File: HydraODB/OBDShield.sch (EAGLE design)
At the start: 10 parts, among them J1 HYDRABUS_SHIELD_CON_HEADER_2X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, J2 HYDRABUS_SHIELD_CON_HEADER_2X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, J3 HYDRABUS_SHIELD_CON_HEADER_2X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, U1 SN65HVD233DG4, U2 SN65HVD233DG4

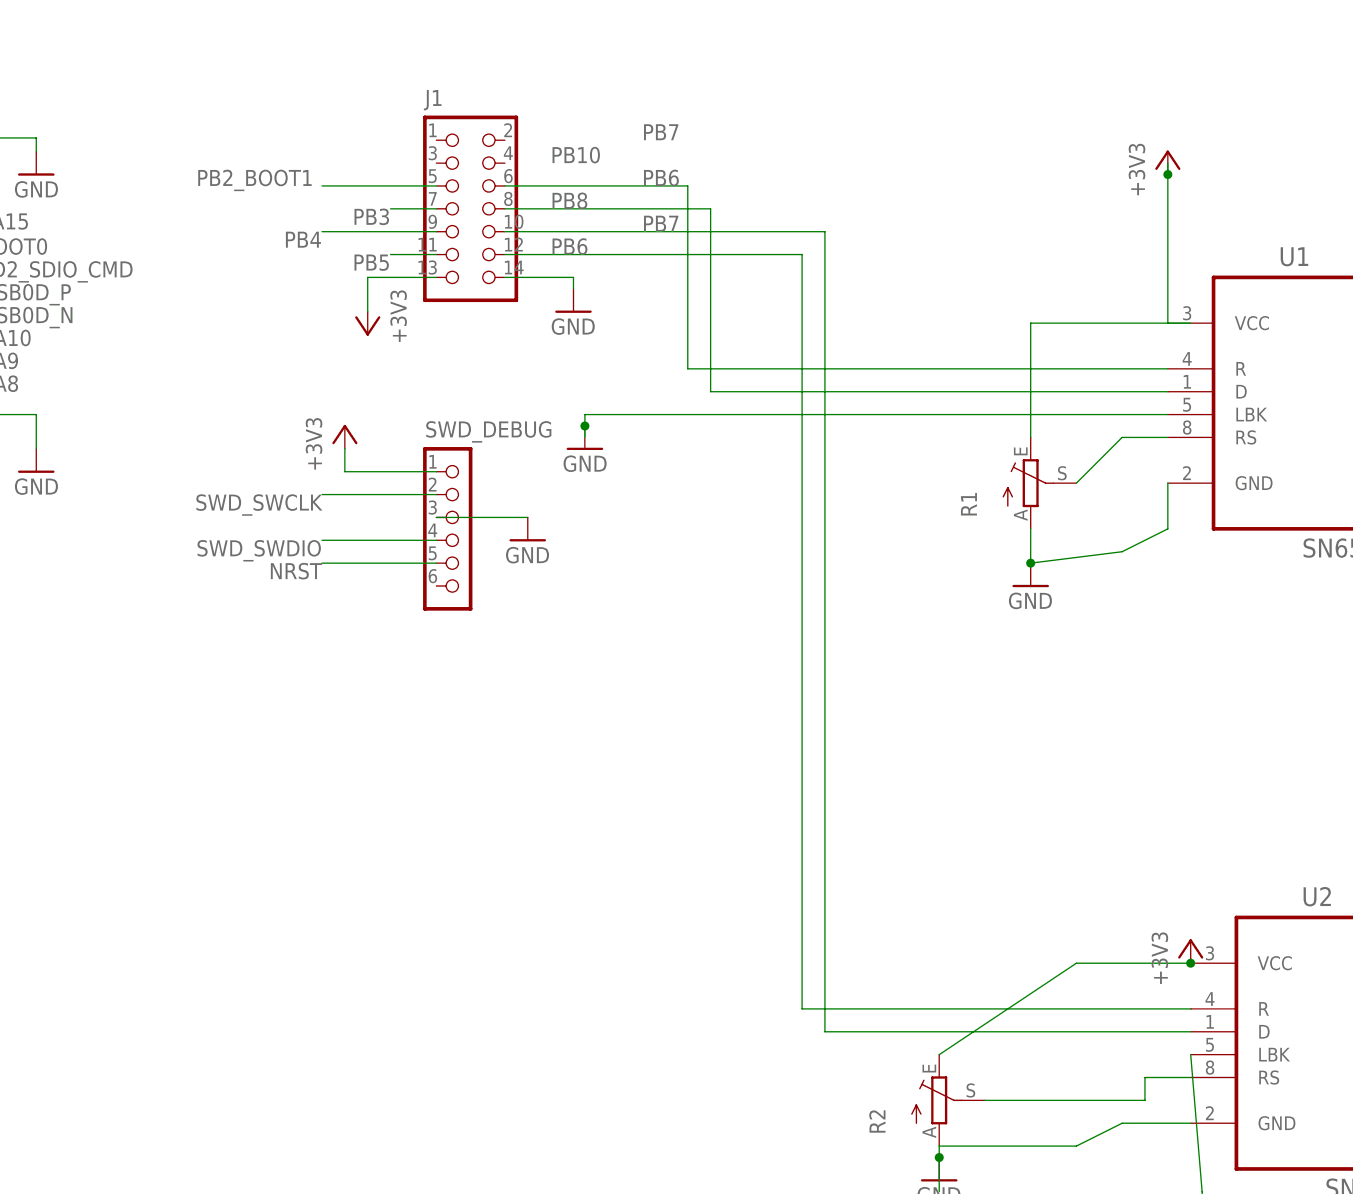
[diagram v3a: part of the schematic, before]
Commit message: Schema correction
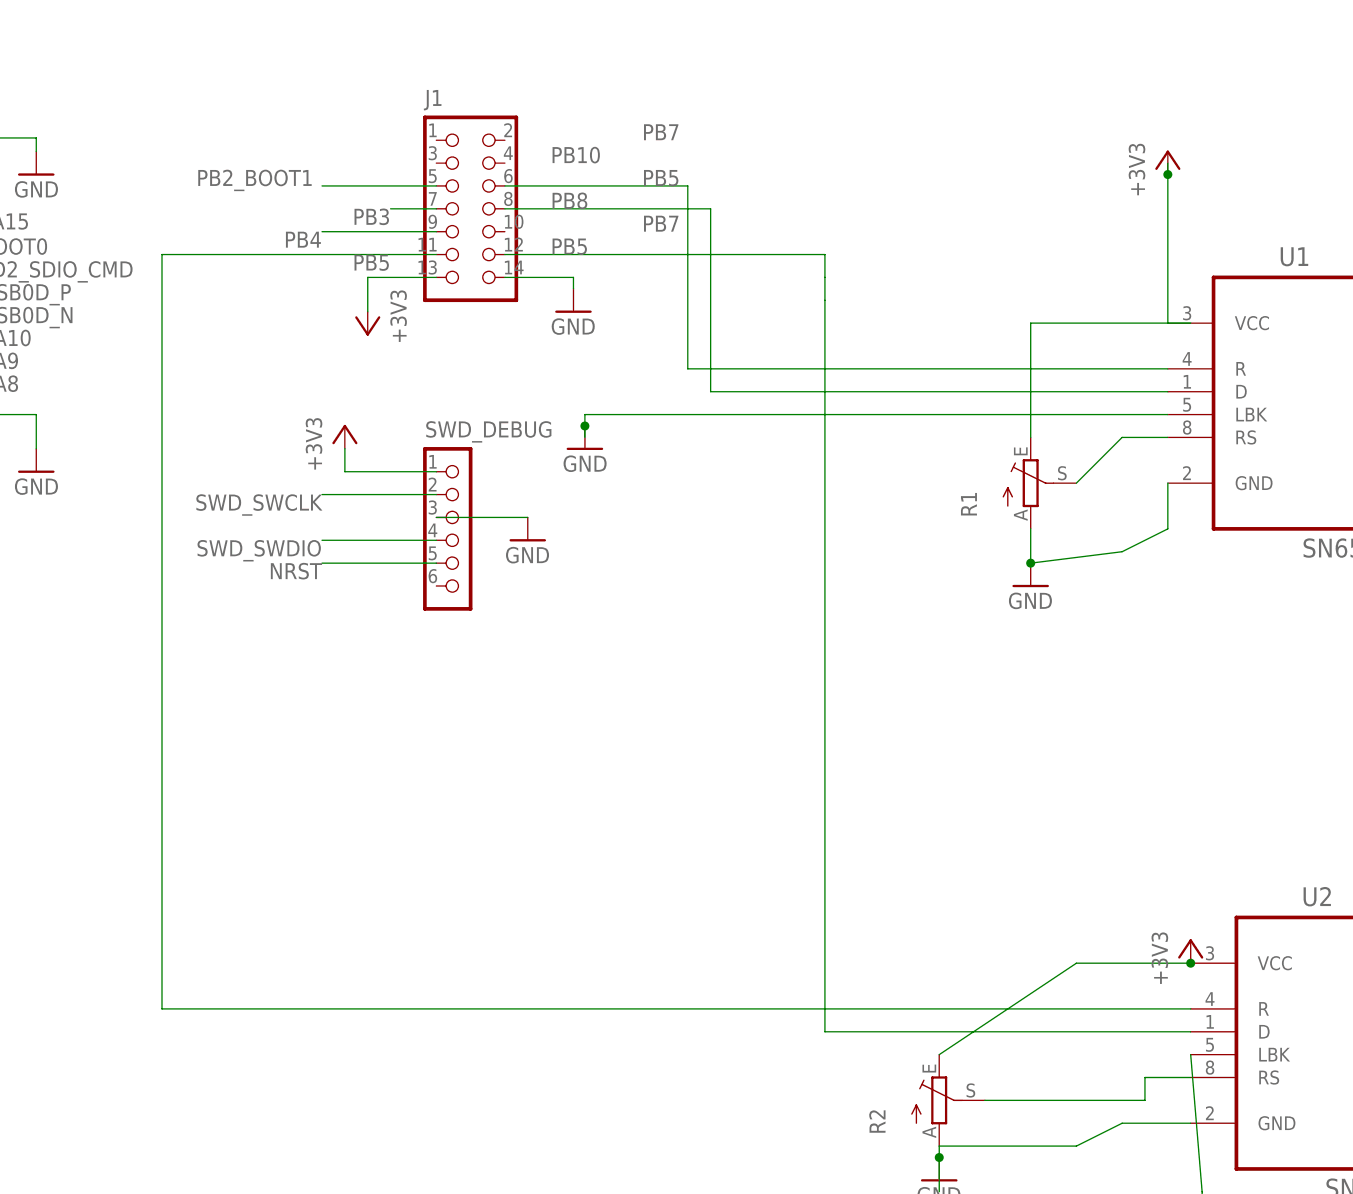
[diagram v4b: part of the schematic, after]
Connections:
- removed net PB6: J1.12, U2.R
- net PB5: now also U2.R
- net PB7: now also J1.12; no longer J1.10
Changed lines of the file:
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@@
-</segment>
-</net>
-<net name="PB5" class="0">
-<segment>
-<wire x1="76.2" y1="121.92" x2="71.12" y2="121.92" width="0.1524" layer="91"/>
-<label x="71.12" y="121.92" size="1.778" layer="95" rot="R180"/>
-<pinref part="J1" gate="J" pin="11"/>
 </segment>
 </net>
@@
 </segment>
 </net>
-<net name="PB6" class="0">
-<segment>
-<label x="99.06" y="129.54" size="1.778" layer="95"/>
-<pinref part="U2" gate="A" pin="R"/>
-<wire x1="160.02" y1="38.1" x2="116.84" y2="38.1" width="0.1524" layer="91"/>
-<wire x1="116.84" y1="38.1" x2="116.84" y2="121.92" width="0.1524" layer="91"/>
-<label x="88.9" y="121.92" size="1.778" layer="95"/>
-<pinref part="J1" gate="J" pin="12"/>
-<wire x1="116.84" y1="121.92" x2="83.82" y2="121.92" width="0.1524" layer="91"/>
-</segment>
-</net>
 <net name="PB7" class="0">
 <segment>
@@
 <pinref part="U2" gate="A" pin="D"/>
 <wire x1="160.02" y1="35.56" x2="119.38" y2="35.56" width="0.1524" layer="91"/>
-<wire x1="119.38" y1="35.56" x2="119.38" y2="124.46" width="0.1524" layer="91"/>
+<wire x1="119.38" y1="35.56" x2="119.38" y2="116.84" width="0.1524" layer="91"/>
 <label x="99.06" y="124.46" size="1.778" layer="95"/>
-<pinref part="J1" gate="J" pin="10"/>
-<wire x1="119.38" y1="124.46" x2="83.82" y2="124.46" width="0.1524" layer="91"/>
+<pinref part="J1" gate="J" pin="12"/>
+<wire x1="119.38" y1="116.84" x2="119.38" y2="119.38" width="0.1524" layer="91"/>
+<wire x1="83.82" y1="121.92" x2="119.38" y2="121.92" width="0.1524" layer="91"/>
+<wire x1="119.38" y1="121.92" x2="119.38" y2="119.38" width="0.1524" layer="91"/>
 </segment>
 </net>
+<net name="PB5" class="0">
+<segment>
+<label x="99.06" y="129.54" size="1.778" layer="95"/>
+<pinref part="U2" gate="A" pin="R"/>
+<wire x1="160.02" y1="38.1" x2="45.72" y2="38.1" width="0.1524" layer="91"/>
+<label x="88.9" y="121.92" size="1.778" layer="95"/>
+<wire x1="45.72" y1="38.1" x2="45.72" y2="121.92" width="0.1524" layer="91"/>
+<label x="71.12" y="121.92" size="1.778" layer="95" rot="R180"/>
+<pinref part="J1" gate="J" pin="11"/>
+<wire x1="45.72" y1="121.92" x2="76.2" y2="121.92" width="0.1524" layer="91"/>
+</segment>
+</net>

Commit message: Mistake :-D
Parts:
- added JP1, JP2: (no value), jumper:JP1E
- added LPWR, LRXCAN1, LRXCAN2, LTXCAN1, LTXCAN2: (no value), led:LEDCHIPLED_0603
- added R3, R4, R5, R6, R7, R8, R9: (no value), resistor:R-EU_R0603
- IC1: value (none) -> LM317MABDT; device v-reg:78XXS -> v-reg:LM317MABDT
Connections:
- new net N$13: LTXCAN1.A, R5.2
- new net N$14: LPWR.A, R3.1
- new net N$15: R3.2
- new net N$16: JP2.1, R9.2
- new net N$19: JP1.1, R8.2
- new net N$7: LRXCAN1.A, R4.2
- new net PB11: J1.4, R9.1, U2.D
- new net PB6: J1.12
- new net PB9: J1.2, JP2.2, U2.R
- net +12V: now also SV1.7, SV1.8
- net GND: now also IC1.ADJ, LPWR.C, LTXCAN1.C; no longer IC1.GND
- net PB10: now also J1.6, JP1.2, R5.1; no longer J1.8
- net PB5: no longer U2.R
- net PB7: now also J1.10; no longer J1.12, U2.D
- net PB8: now also J1.8, R4.1, R8.1; no longer J1.6
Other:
- moved on the sheet: R2, SV1

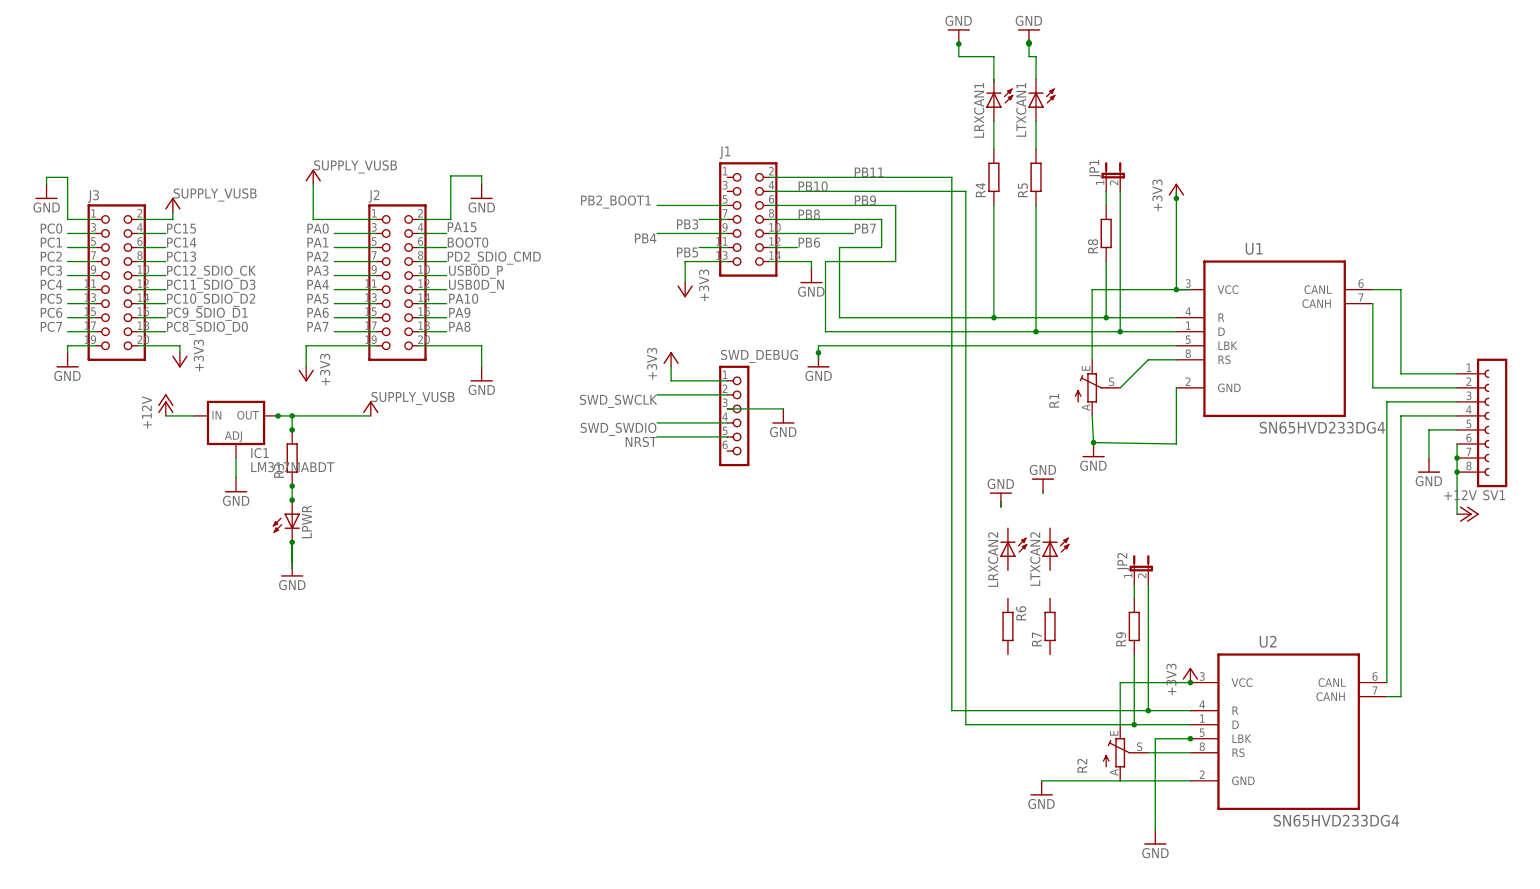
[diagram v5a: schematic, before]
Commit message: Decoupling caps, user button and different mistakes
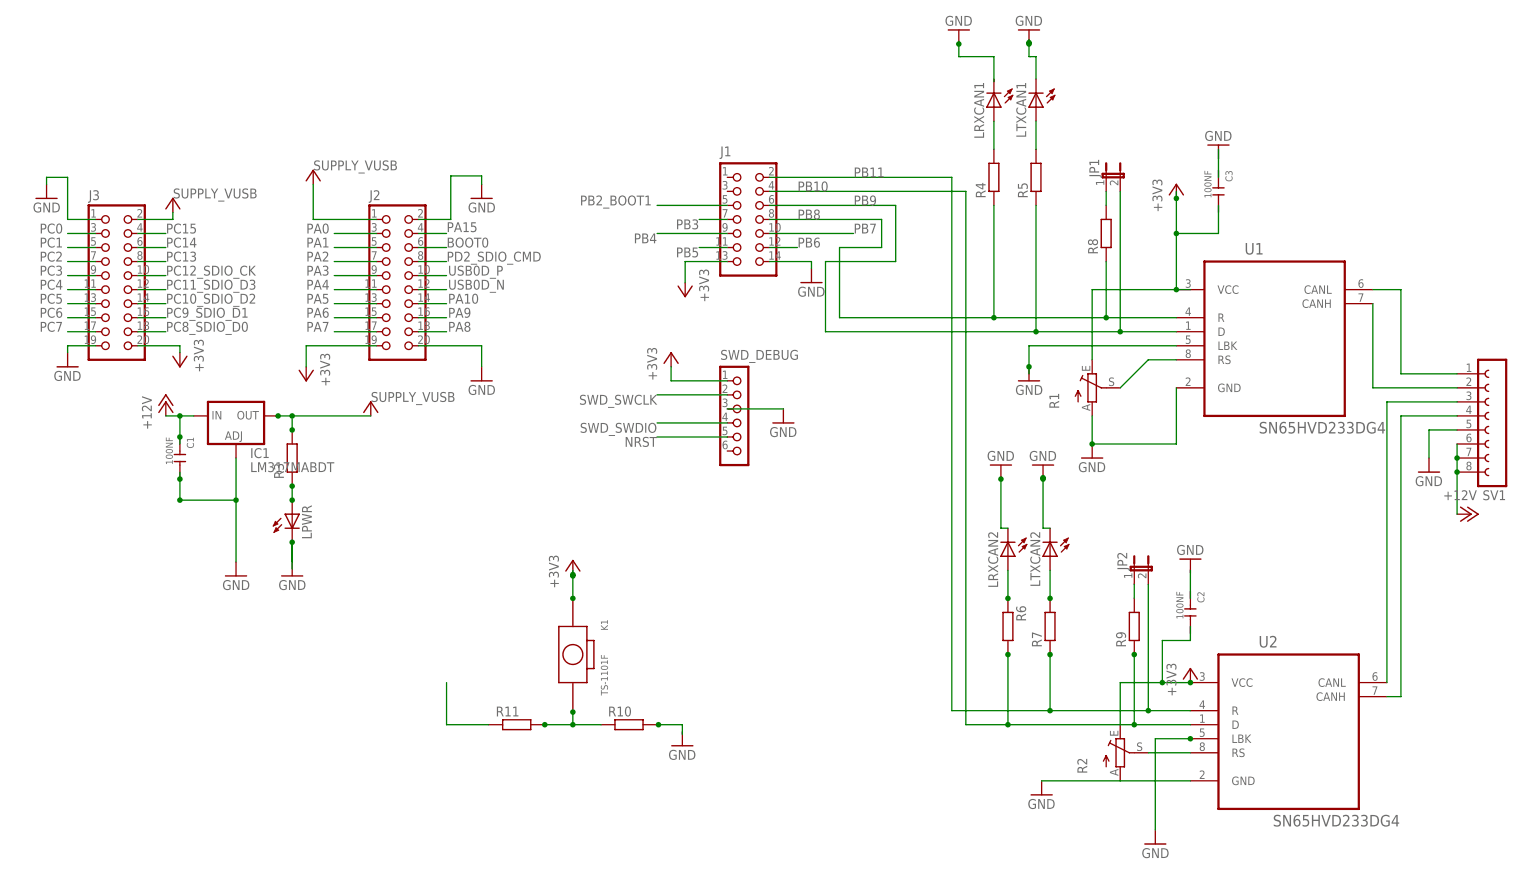
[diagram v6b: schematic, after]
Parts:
- added C1, C2, C3: 100NF, Seeed-OPL-Capacitor:CERAMIC-100NF-50V-20%-Y5V(0805)
- added K1: TS-1101F, Seeed-OPL-Button:DIP-BUTTON-FRONT-WHITE(2P-3.4X6MM)
- added R10, R11: (no value), resistor:R-EU_R0603
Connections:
- new net N$21: K1.2, R10.1, R11.2
- new net N$22: R10.2
- new net N$4: LRXCAN2.A, R6.1
- new net N$6: LTXCAN2.A, R7.2
- net +12V: now also C1.1
- net +3V3: now also K1.1
- net GND: now also C1.2, LRXCAN2.C, LTXCAN2.C
- net PB11: now also R6.2
- net PB7: now also R11.1
- net PB9: now also R7.1

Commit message: Different corrections and missing wire
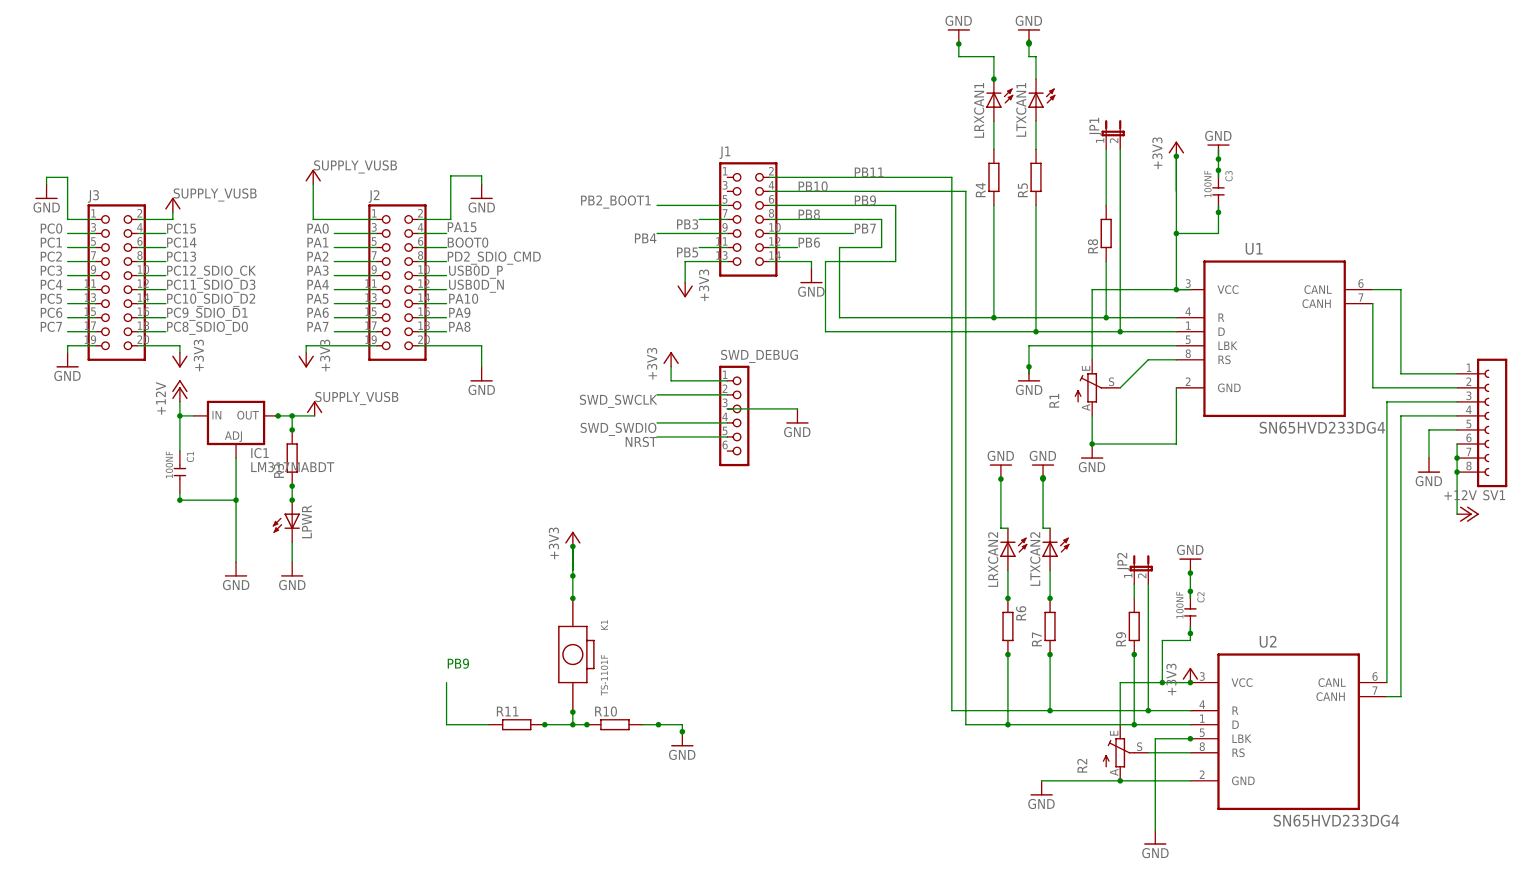
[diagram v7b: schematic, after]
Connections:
- removed net N$22: R10.2
- net +3V3: now also C2.2, C3.2
- net GND: now also C2.1, C3.1, LRXCAN1.C, R10.2
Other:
- note added: "PB9"
- moved on the sheet: C1, JP1, R10
